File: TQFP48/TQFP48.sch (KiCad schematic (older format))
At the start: 5 parts, among them J1 Conn_01x24, J2 Conn_02x24_Counter_Clockwise, J3 Conn_02x24_Counter_Clockwise, J4 Conn_01x24, J5 Conn_01x05

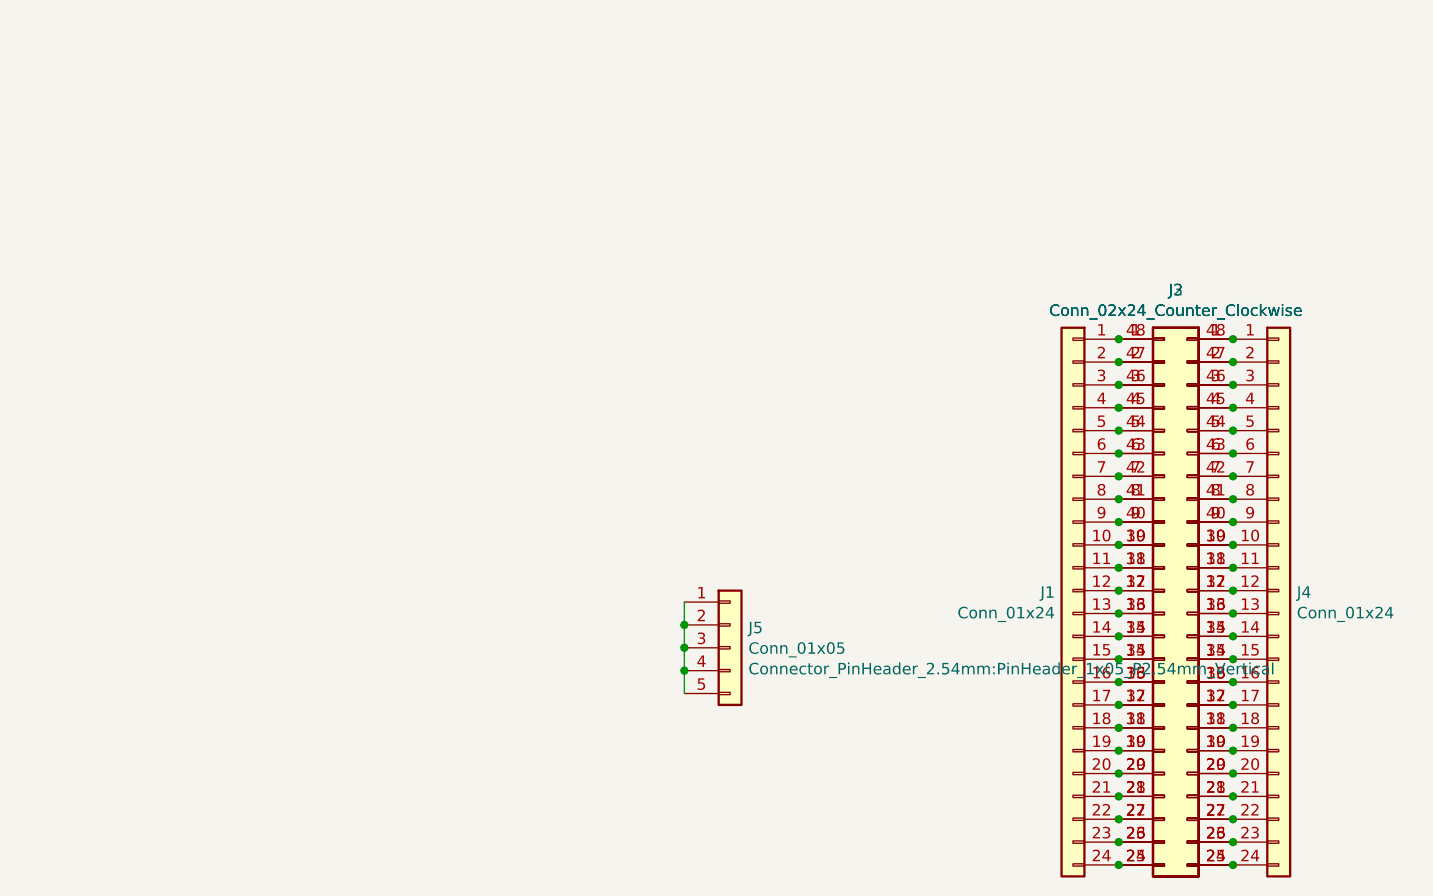
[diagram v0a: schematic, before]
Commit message: USB, SD and CR Cells Added
MicroSD, MicroUSB, MiniUSB, USB-C, CR1220, CR2032 added as well as all schematics page sizes optimised
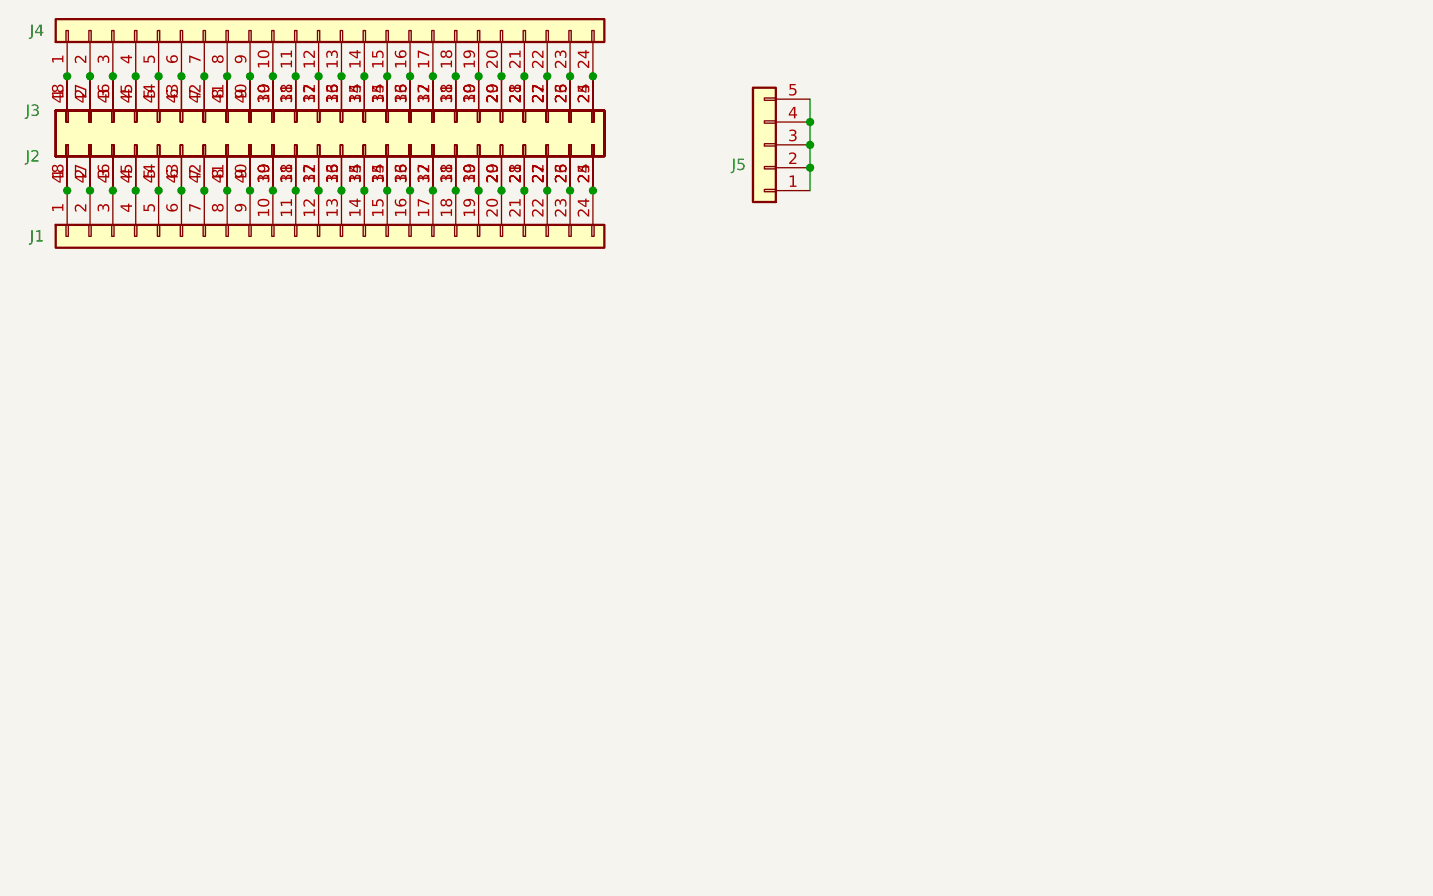
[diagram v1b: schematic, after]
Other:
- moved on the sheet: J1, J2, J3, J4, J5
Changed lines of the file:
@@
 EELAYER 29 0
 EELAYER END
-$Descr A4 11693 8268
+$Descr User 5197 4016
 encoding utf-8
 Sheet 1 1
-Title ""
-Date ""
-Rev ""
-Comp ""
-Comment1 ""
-Comment2 ""
-Comment3 ""
+Title "TQFP48 to DIP48 Breakout Board"
+Date "2019-07-24"
+Rev "1"
+Comp "SirBoard"
+Comment1 "TQFP48 P = 0.5mm"
+Comment2 "QFN48 P = 0.4mm"
+Comment3 "DIP48 P = 2.54mm"
 Comment4 ""
 $EndDescr
@@
 L Connector_Generic:Conn_01x24 J1
 U 1 1 5D370B07
-P 5400 3450
-F 0 "J1" H 5479 3442 50  0000 L CNN
-F 1 "Conn_01x24" H 5479 3352 50  0000 L CNN
-F 2 "Connector_PinHeader_2.54mm:PinHeader_1x24_P2.54mm_Vertical" H 5400 3450 50  0001 C CNN
-F 3 "~" H 5400 3450 50  0001 C CNN
-	1    5400 3450
-	-1   0    0    -1
+P 2100 1900
+F 0 "J1" V 2100 3100 50  0000 L CNN
+F 1 "Conn_01x24" H 2179 1802 50  0001 L CNN
+F 2 "Connector_PinHeader_2.54mm:PinHeader_1x24_P2.54mm_Vertical" H 2100 1900 50  0001 C CNN
+F 3 "~" H 2100 1900 50  0001 C CNN
+	1    2100 1900
+	0    -1   1    0
 $EndComp
 $Comp
 L Connector_Generic:Conn_02x24_Counter_Clockwise J2
 U 1 1 5D3711C0
-P 5800 3450
-F 0 "J2" H 5850 4765 50  0000 C CNN
-F 1 "Conn_02x24_Counter_Clockwise" H 5850 4675 50  0000 C CNN
-F 2 "Package_QFP:TQFP-48-1EP_7x7mm_P0.5mm_EP5x5mm" H 5800 3450 50  0001 C CNN
-F 3 "~" H 5800 3450 50  0001 C CNN
-	1    5800 3450
-	1    0    0    -1
+P 2100 1500
+F 0 "J2" V 2050 2750 50  0000 C CNN
+F 1 "Conn_02x24_Counter_Clockwise" H 2150 2725 50  0001 C CNN
+F 2 "Package_QFP:TQFP-48-1EP_7x7mm_P0.5mm_EP5x5mm" H 2100 1500 50  0001 C CNN
+F 3 "~" H 2100 1500 50  0001 C CNN
+	1    2100 1500
+	0    -1   -1   0
 $EndComp
 $Comp
 L Connector_Generic:Conn_01x24 J4
 U 1 1 5D373583
-P 6300 3450
-F 0 "J4" H 6379 3442 50  0000 L CNN
-F 1 "Conn_01x24" H 6379 3352 50  0000 L CNN
-F 2 "Connector_PinHeader_2.54mm:PinHeader_1x24_P2.54mm_Vertical" H 6300 3450 50  0001 C CNN
-F 3 "~" H 6300 3450 50  0001 C CNN
-	1    6300 3450
-	1    0    0    -1
+P 2100 1000
+F 0 "J4" V 2100 2200 50  0000 L CNN
+F 1 "Conn_01x24" H 2179 902 50  0001 L CNN
+F 2 "Connector_PinHeader_2.54mm:PinHeader_1x24_P2.54mm_Vertical" H 2100 1000 50  0001 C CNN
+F 3 "~" H 2100 1000 50  0001 C CNN
+	1    2100 1000
+	0    -1   -1   0
 $EndComp
 $Comp
 L Connector_Generic:Conn_02x24_Counter_Clockwise J3
 U 1 1 5D376148
-P 5900 3450
-F 0 "J3" H 5950 4765 50  0000 C CNN
-F 1 "Conn_02x24_Counter_Clockwise" H 5950 4675 50  0000 C CNN
-F 2 "Package_DFN_QFN:UQFN-48-1EP_6x6mm_P0.4mm_EP4.62x4.62mm" H 5900 3450 50  0001 C CNN
-F 3 "~" H 5900 3450 50  0001 C CNN
-	1    5900 3450
-	-1   0    0    -1
+P 2100 1400
+F 0 "J3" V 2050 2650 50  0000 C CNN
+F 1 "Conn_02x24_Counter_Clockwise" H 2150 2625 50  0001 C CNN
+F 2 "Package_DFN_QFN:UQFN-48-1EP_6x6mm_P0.4mm_EP4.62x4.62mm" H 2100 1400 50  0001 C CNN
+F 3 "~" H 2100 1400 50  0001 C CNN
+	1    2100 1400
+	0    -1   1    0
 $EndComp
-Connection ~ 5600 2350
-Connection ~ 5600 2450
-Connection ~ 5600 2550
-Connection ~ 5600 2650
-Connection ~ 5600 2750
-Connection ~ 5600 2850
-Connection ~ 5600 2950
-Connection ~ 5600 3050
-Connection ~ 5600 3150
-Connection ~ 5600 3250
-Connection ~ 5600 3350
-Connection ~ 5600 3450
-Connection ~ 5600 3550
-Connection ~ 5600 3650
-Connection ~ 5600 3750
-Connection ~ 5600 3850
-Connection ~ 5600 3950
-Connection ~ 5600 4050
-Connection ~ 5600 4150
-Connection ~ 5600 4250
-Connection ~ 5600 4350
-Connection ~ 5600 4450
-Connection ~ 5600 4550
-Connection ~ 5600 4650
-Connection ~ 6100 2350
-Connection ~ 6100 2450
-Connection ~ 6100 2550
-Connection ~ 6100 2650
-Connection ~ 6100 2750
-Connection ~ 6100 2850
-Connection ~ 6100 2950
-Connection ~ 6100 3050
-Connection ~ 6100 3150
-Connection ~ 6100 3250
-Connection ~ 6100 3350
-Connection ~ 6100 3450
-Connection ~ 6100 3550
-Connection ~ 6100 3650
-Connection ~ 6100 3750
-Connection ~ 6100 3850
-Connection ~ 6100 3950
-Connection ~ 6100 4050
-Connection ~ 6100 4150
-Connection ~ 6100 4250
-Connection ~ 6100 4350
-Connection ~ 6100 4450
-Connection ~ 6100 4550
-Connection ~ 6100 4650
+Connection ~ 1000 1700
+Connection ~ 1100 1700
+Connection ~ 1200 1700
+Connection ~ 1300 1700
+Connection ~ 1400 1700
+Connection ~ 1500 1700
+Connection ~ 1600 1700
+Connection ~ 1700 1700
+Connection ~ 1800 1700
+Connection ~ 1900 1700
+Connection ~ 2000 1700
+Connection ~ 2100 1700
+Connection ~ 2200 1700
+Connection ~ 2300 1700
+Connection ~ 2400 1700
+Connection ~ 2500 1700
+Connection ~ 2600 1700
+Connection ~ 2700 1700
+Connection ~ 2800 1700
+Connection ~ 2900 1700
+Connection ~ 3000 1700
+Connection ~ 3100 1700
+Connection ~ 3200 1700
+Connection ~ 3300 1700
+Connection ~ 1000 1200
+Connection ~ 1100 1200
+Connection ~ 1200 1200
+Connection ~ 1300 1200
+Connection ~ 1400 1200
+Connection ~ 1500 1200
+Connection ~ 1600 1200
+Connection ~ 1700 1200
+Connection ~ 1800 1200
+Connection ~ 1900 1200
+Connection ~ 2000 1200
+Connection ~ 2100 1200
+Connection ~ 2200 1200
+Connection ~ 2300 1200
+Connection ~ 2400 1200
+Connection ~ 2500 1200
+Connection ~ 2600 1200
+Connection ~ 2700 1200
+Connection ~ 2800 1200
+Connection ~ 2900 1200
+Connection ~ 3000 1200
+Connection ~ 3100 1200
+Connection ~ 3200 1200
+Connection ~ 3300 1200
 $Comp
 L Connector_Generic:Conn_01x05 J5
 U 1 1 5D399F66
-P 3900 3700
-F 0 "J5" H 3980 3787 50  0000 L CNN
-F 1 "Conn_01x05" H 3980 3697 50  0000 L CNN
-F 2 "Connector_PinHeader_2.54mm:PinHeader_1x05_P2.54mm_Vertical" H 3980 3607 50  0000 L CNN
-F 3 "~" H 3900 3700 50  0001 C CNN
-	1    3900 3700
-	1    0    0    -1
+P 4050 1500
+F 0 "J5" H 4130 1587 50  0000 L CNN
+F 1 "Conn_01x05" H 4130 1497 50  0001 L CNN
+F 2 "Connector_PinHeader_2.54mm:PinHeader_1x05_P2.54mm_Vertical" H 4130 1407 50  0001 L CNN
+F 3 "~" H 4050 1500 50  0001 C CNN
+	1    4050 1500
+	-1   0    0    1
 $EndComp
 Wire Wire Line
-	3700 3500 3700 3600
-Connection ~ 3700 3600
+	4250 1700 4250 1600
+Connection ~ 4250 1600
 Wire Wire Line
-	3700 3600 3700 3700
-Connection ~ 3700 3700
+	4250 1600 4250 1500
+Connection ~ 4250 1500
 Wire Wire Line
-	3700 3700 3700 3800
-Connection ~ 3700 3800
+	4250 1500 4250 1400
+Connection ~ 4250 1400
 Wire Wire Line
-	3700 3800 3700 3900
+	4250 1400 4250 1300
 $EndSCHEMATC
